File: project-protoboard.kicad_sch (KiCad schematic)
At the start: 8 parts, among them J1 Conn_01x07_Socket, J2 Conn_01x30_Socket, J3 SM04B-SRSS-TB(LF)(SN), J4 Conn_01x05_Socket

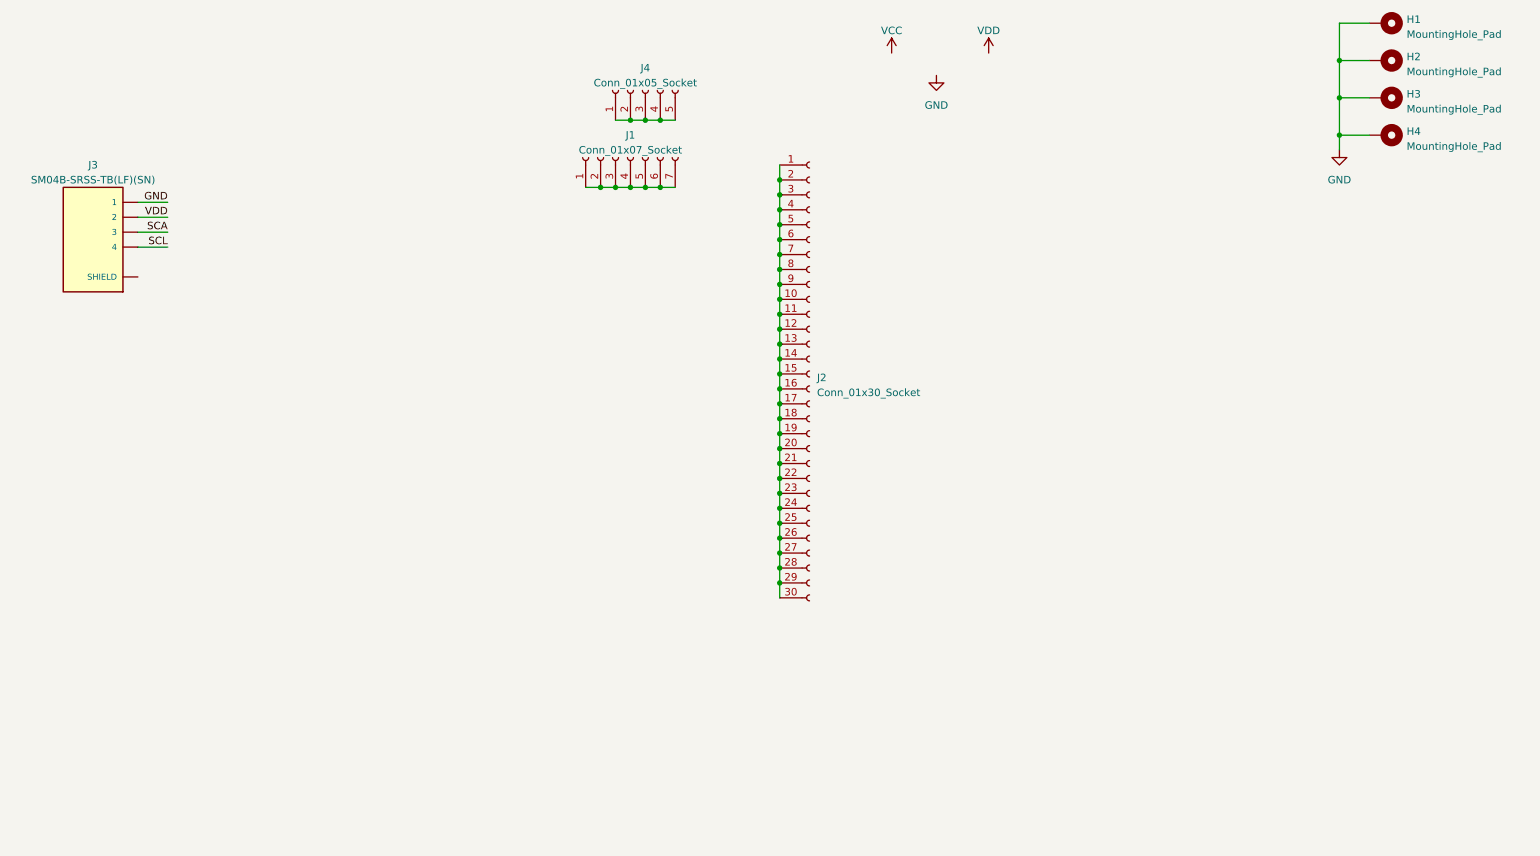
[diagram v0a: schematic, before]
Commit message: Placement and board edge done
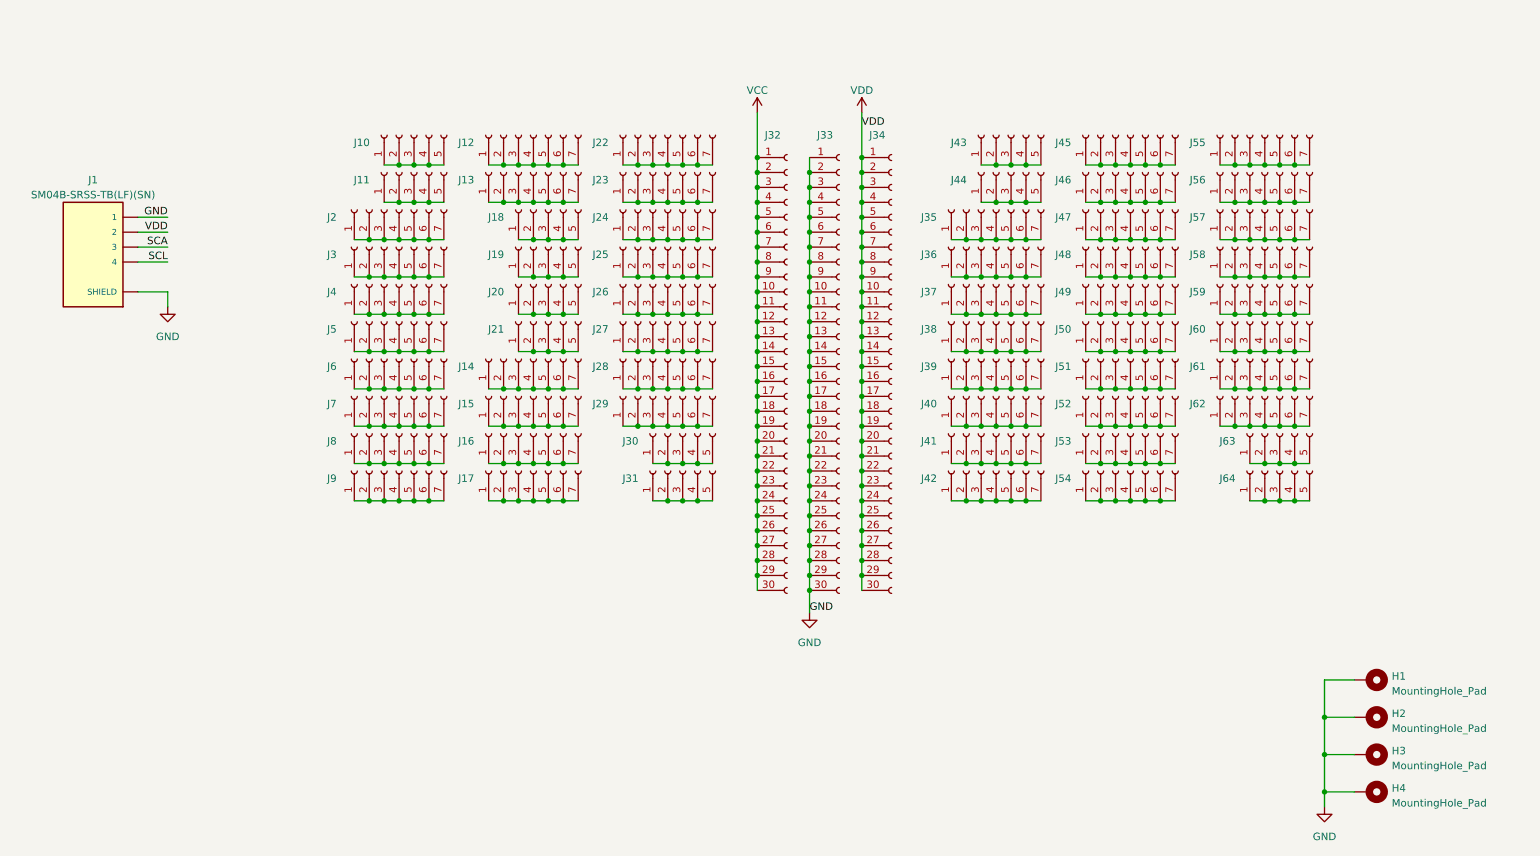
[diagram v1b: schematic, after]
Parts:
- removed J1: Conn_01x07_Socket, Proto:Proto_1x07_P2.54mm, symbol Connector:Conn_01x07_Socket
- added J10, J18, J19, J20, J21, J30, J31, J43, J44, J63, J64: Conn_01x05_Socket, Proto:Proto_1x05_P2.54mm, symbol Connector:Conn_01x05_Socket
- added J12, J13, J14, J15, J16, J17, J2, J22, J23, J24, J25, J26, J27, J28, J29, J3, J35, J36, J37, J38, J39, J4, J40, J41, J42, J45, J46, J47, J48, J49, J5, J50, J51, J52, J53, J54, J55, J56, J57, J58, J59, J6, J60, J61, J62, J7, J8, J9: Conn_01x07_Socket, Proto:Proto_1x07_P2.54mm, symbol Connector:Conn_01x07_Socket
- added J32, J34: Conn_01x30_Socket, Proto:Proto_1x30_P2.54mm, symbol Connector:Conn_01x30_Socket
- renumbered J3 to J1, J4 to J11, J2 to J33
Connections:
- net GND: now also J1.S1 (SHIELD), J1.S2 (SHIELD), J33.1 (Pin_1), J33.10 (Pin_10), J33.11 (Pin_11), J33.12 (Pin_12), J33.13 (Pin_13), J33.14 (Pin_14), J33.15 (Pin_15), J33.16 (Pin_16), J33.17 (Pin_17), J33.18 (Pin_18), J33.19 (Pin_19), J33.2 (Pin_2), J33.20 (Pin_20), J33.21 (Pin_21), J33.22 (Pin_22), J33.23 (Pin_23), J33.24 (Pin_24), J33.25 (Pin_25), J33.26 (Pin_26), J33.27 (Pin_27), J33.28 (Pin_28), J33.29 (Pin_29), J33.3 (Pin_3), J33.30 (Pin_30), J33.4 (Pin_4), J33.5 (Pin_5), J33.6 (Pin_6), J33.7 (Pin_7), J33.8 (Pin_8), J33.9 (Pin_9)
- net VCC: now also J32.1 (Pin_1), J32.10 (Pin_10), J32.11 (Pin_11), J32.12 (Pin_12), J32.13 (Pin_13), J32.14 (Pin_14), J32.15 (Pin_15), J32.16 (Pin_16), J32.17 (Pin_17), J32.18 (Pin_18), J32.19 (Pin_19), J32.2 (Pin_2), J32.20 (Pin_20), J32.21 (Pin_21), J32.22 (Pin_22), J32.23 (Pin_23), J32.24 (Pin_24), J32.25 (Pin_25), J32.26 (Pin_26), J32.27 (Pin_27), J32.28 (Pin_28), J32.29 (Pin_29), J32.3 (Pin_3), J32.30 (Pin_30), J32.4 (Pin_4), J32.5 (Pin_5), J32.6 (Pin_6), J32.7 (Pin_7), J32.8 (Pin_8), J32.9 (Pin_9)
- net VDD: now also J34.1 (Pin_1), J34.10 (Pin_10), J34.11 (Pin_11), J34.12 (Pin_12), J34.13 (Pin_13), J34.14 (Pin_14), J34.15 (Pin_15), J34.16 (Pin_16), J34.17 (Pin_17), J34.18 (Pin_18), J34.19 (Pin_19), J34.2 (Pin_2), J34.20 (Pin_20), J34.21 (Pin_21), J34.22 (Pin_22), J34.23 (Pin_23), J34.24 (Pin_24), J34.25 (Pin_25), J34.26 (Pin_26), J34.27 (Pin_27), J34.28 (Pin_28), J34.29 (Pin_29), J34.3 (Pin_3), J34.30 (Pin_30), J34.4 (Pin_4), J34.5 (Pin_5), J34.6 (Pin_6), J34.7 (Pin_7), J34.8 (Pin_8), J34.9 (Pin_9)
- new net: J39.1 (Pin_1), J39.2 (Pin_2), J39.3 (Pin_3), J39.4 (Pin_4), J39.5 (Pin_5), J39.6 (Pin_6), J39.7 (Pin_7)
- new net: J47.1 (Pin_1), J47.2 (Pin_2), J47.3 (Pin_3), J47.4 (Pin_4), J47.5 (Pin_5), J47.6 (Pin_6), J47.7 (Pin_7)
- new net: J24.1 (Pin_1), J24.2 (Pin_2), J24.3 (Pin_3), J24.4 (Pin_4), J24.5 (Pin_5), J24.6 (Pin_6), J24.7 (Pin_7)
- new net: J30.1 (Pin_1), J30.2 (Pin_2), J30.3 (Pin_3), J30.4 (Pin_4), J30.5 (Pin_5)
- new net: J17.1 (Pin_1), J17.2 (Pin_2), J17.3 (Pin_3), J17.4 (Pin_4), J17.5 (Pin_5), J17.6 (Pin_6), J17.7 (Pin_7)
- new net: J14.1 (Pin_1), J14.2 (Pin_2), J14.3 (Pin_3), J14.4 (Pin_4), J14.5 (Pin_5), J14.6 (Pin_6), J14.7 (Pin_7)
- new net: J62.1 (Pin_1), J62.2 (Pin_2), J62.3 (Pin_3), J62.4 (Pin_4), J62.5 (Pin_5), J62.6 (Pin_6), J62.7 (Pin_7)
- new net: J38.1 (Pin_1), J38.2 (Pin_2), J38.3 (Pin_3), J38.4 (Pin_4), J38.5 (Pin_5), J38.6 (Pin_6), J38.7 (Pin_7)
- new net: J23.1 (Pin_1), J23.2 (Pin_2), J23.3 (Pin_3), J23.4 (Pin_4), J23.5 (Pin_5), J23.6 (Pin_6), J23.7 (Pin_7)
- new net: J6.1 (Pin_1), J6.2 (Pin_2), J6.3 (Pin_3), J6.4 (Pin_4), J6.5 (Pin_5), J6.6 (Pin_6), J6.7 (Pin_7)
- new net: J53.1 (Pin_1), J53.2 (Pin_2), J53.3 (Pin_3), J53.4 (Pin_4), J53.5 (Pin_5), J53.6 (Pin_6), J53.7 (Pin_7)
- new net: J55.1 (Pin_1), J55.2 (Pin_2), J55.3 (Pin_3), J55.4 (Pin_4), J55.5 (Pin_5), J55.6 (Pin_6), J55.7 (Pin_7)
- new net: J3.1 (Pin_1), J3.2 (Pin_2), J3.3 (Pin_3), J3.4 (Pin_4), J3.5 (Pin_5), J3.6 (Pin_6), J3.7 (Pin_7)
- new net: J64.1 (Pin_1), J64.2 (Pin_2), J64.3 (Pin_3), J64.4 (Pin_4), J64.5 (Pin_5)
- new net: J7.1 (Pin_1), J7.2 (Pin_2), J7.3 (Pin_3), J7.4 (Pin_4), J7.5 (Pin_5), J7.6 (Pin_6), J7.7 (Pin_7)
- new net: J25.1 (Pin_1), J25.2 (Pin_2), J25.3 (Pin_3), J25.4 (Pin_4), J25.5 (Pin_5), J25.6 (Pin_6), J25.7 (Pin_7)
- new net: J42.1 (Pin_1), J42.2 (Pin_2), J42.3 (Pin_3), J42.4 (Pin_4), J42.5 (Pin_5), J42.6 (Pin_6), J42.7 (Pin_7)
- new net: J12.1 (Pin_1), J12.2 (Pin_2), J12.3 (Pin_3), J12.4 (Pin_4), J12.5 (Pin_5), J12.6 (Pin_6), J12.7 (Pin_7)
- new net: J57.1 (Pin_1), J57.2 (Pin_2), J57.3 (Pin_3), J57.4 (Pin_4), J57.5 (Pin_5), J57.6 (Pin_6), J57.7 (Pin_7)
- new net: J19.1 (Pin_1), J19.2 (Pin_2), J19.3 (Pin_3), J19.4 (Pin_4), J19.5 (Pin_5)
- new net: J4.1 (Pin_1), J4.2 (Pin_2), J4.3 (Pin_3), J4.4 (Pin_4), J4.5 (Pin_5), J4.6 (Pin_6), J4.7 (Pin_7)
- new net: J43.1 (Pin_1), J43.2 (Pin_2), J43.3 (Pin_3), J43.4 (Pin_4), J43.5 (Pin_5)
- new net: J48.1 (Pin_1), J48.2 (Pin_2), J48.3 (Pin_3), J48.4 (Pin_4), J48.5 (Pin_5), J48.6 (Pin_6), J48.7 (Pin_7)
- new net: J50.1 (Pin_1), J50.2 (Pin_2), J50.3 (Pin_3), J50.4 (Pin_4), J50.5 (Pin_5), J50.6 (Pin_6), J50.7 (Pin_7)
- new net: J46.1 (Pin_1), J46.2 (Pin_2), J46.3 (Pin_3), J46.4 (Pin_4), J46.5 (Pin_5), J46.6 (Pin_6), J46.7 (Pin_7)
- new net: J54.1 (Pin_1), J54.2 (Pin_2), J54.3 (Pin_3), J54.4 (Pin_4), J54.5 (Pin_5), J54.6 (Pin_6), J54.7 (Pin_7)
- new net: J5.1 (Pin_1), J5.2 (Pin_2), J5.3 (Pin_3), J5.4 (Pin_4), J5.5 (Pin_5), J5.6 (Pin_6), J5.7 (Pin_7)
- new net: J52.1 (Pin_1), J52.2 (Pin_2), J52.3 (Pin_3), J52.4 (Pin_4), J52.5 (Pin_5), J52.6 (Pin_6), J52.7 (Pin_7)
- new net: J16.1 (Pin_1), J16.2 (Pin_2), J16.3 (Pin_3), J16.4 (Pin_4), J16.5 (Pin_5), J16.6 (Pin_6), J16.7 (Pin_7)
- new net: J59.1 (Pin_1), J59.2 (Pin_2), J59.3 (Pin_3), J59.4 (Pin_4), J59.5 (Pin_5), J59.6 (Pin_6), J59.7 (Pin_7)
- new net: J63.1 (Pin_1), J63.2 (Pin_2), J63.3 (Pin_3), J63.4 (Pin_4), J63.5 (Pin_5)
- new net: J9.1 (Pin_1), J9.2 (Pin_2), J9.3 (Pin_3), J9.4 (Pin_4), J9.5 (Pin_5), J9.6 (Pin_6), J9.7 (Pin_7)
- new net: J35.1 (Pin_1), J35.2 (Pin_2), J35.3 (Pin_3), J35.4 (Pin_4), J35.5 (Pin_5), J35.6 (Pin_6), J35.7 (Pin_7)
- new net: J29.1 (Pin_1), J29.2 (Pin_2), J29.3 (Pin_3), J29.4 (Pin_4), J29.5 (Pin_5), J29.6 (Pin_6), J29.7 (Pin_7)
- new net: J18.1 (Pin_1), J18.2 (Pin_2), J18.3 (Pin_3), J18.4 (Pin_4), J18.5 (Pin_5)
- new net: J20.1 (Pin_1), J20.2 (Pin_2), J20.3 (Pin_3), J20.4 (Pin_4), J20.5 (Pin_5)
- new net: J58.1 (Pin_1), J58.2 (Pin_2), J58.3 (Pin_3), J58.4 (Pin_4), J58.5 (Pin_5), J58.6 (Pin_6), J58.7 (Pin_7)
- new net: J45.1 (Pin_1), J45.2 (Pin_2), J45.3 (Pin_3), J45.4 (Pin_4), J45.5 (Pin_5), J45.6 (Pin_6), J45.7 (Pin_7)
- new net: J15.1 (Pin_1), J15.2 (Pin_2), J15.3 (Pin_3), J15.4 (Pin_4), J15.5 (Pin_5), J15.6 (Pin_6), J15.7 (Pin_7)
- new net: J26.1 (Pin_1), J26.2 (Pin_2), J26.3 (Pin_3), J26.4 (Pin_4), J26.5 (Pin_5), J26.6 (Pin_6), J26.7 (Pin_7)
- new net: J37.1 (Pin_1), J37.2 (Pin_2), J37.3 (Pin_3), J37.4 (Pin_4), J37.5 (Pin_5), J37.6 (Pin_6), J37.7 (Pin_7)
- new net: J31.1 (Pin_1), J31.2 (Pin_2), J31.3 (Pin_3), J31.4 (Pin_4), J31.5 (Pin_5)
- new net: J8.1 (Pin_1), J8.2 (Pin_2), J8.3 (Pin_3), J8.4 (Pin_4), J8.5 (Pin_5), J8.6 (Pin_6), J8.7 (Pin_7)
- new net: J13.1 (Pin_1), J13.2 (Pin_2), J13.3 (Pin_3), J13.4 (Pin_4), J13.5 (Pin_5), J13.6 (Pin_6), J13.7 (Pin_7)
- new net: J44.1 (Pin_1), J44.2 (Pin_2), J44.3 (Pin_3), J44.4 (Pin_4), J44.5 (Pin_5)
- new net: J60.1 (Pin_1), J60.2 (Pin_2), J60.3 (Pin_3), J60.4 (Pin_4), J60.5 (Pin_5), J60.6 (Pin_6), J60.7 (Pin_7)
- new net: J41.1 (Pin_1), J41.2 (Pin_2), J41.3 (Pin_3), J41.4 (Pin_4), J41.5 (Pin_5), J41.6 (Pin_6), J41.7 (Pin_7)
- new net: J21.1 (Pin_1), J21.2 (Pin_2), J21.3 (Pin_3), J21.4 (Pin_4), J21.5 (Pin_5)
- new net: J28.1 (Pin_1), J28.2 (Pin_2), J28.3 (Pin_3), J28.4 (Pin_4), J28.5 (Pin_5), J28.6 (Pin_6), J28.7 (Pin_7)
- new net: J36.1 (Pin_1), J36.2 (Pin_2), J36.3 (Pin_3), J36.4 (Pin_4), J36.5 (Pin_5), J36.6 (Pin_6), J36.7 (Pin_7)
- new net: J40.1 (Pin_1), J40.2 (Pin_2), J40.3 (Pin_3), J40.4 (Pin_4), J40.5 (Pin_5), J40.6 (Pin_6), J40.7 (Pin_7)
- new net: J51.1 (Pin_1), J51.2 (Pin_2), J51.3 (Pin_3), J51.4 (Pin_4), J51.5 (Pin_5), J51.6 (Pin_6), J51.7 (Pin_7)
- new net: J10.1 (Pin_1), J10.2 (Pin_2), J10.3 (Pin_3), J10.4 (Pin_4), J10.5 (Pin_5)
- new net: J61.1 (Pin_1), J61.2 (Pin_2), J61.3 (Pin_3), J61.4 (Pin_4), J61.5 (Pin_5), J61.6 (Pin_6), J61.7 (Pin_7)
- new net: J2.1 (Pin_1), J2.2 (Pin_2), J2.3 (Pin_3), J2.4 (Pin_4), J2.5 (Pin_5), J2.6 (Pin_6), J2.7 (Pin_7)
- new net: J27.1 (Pin_1), J27.2 (Pin_2), J27.3 (Pin_3), J27.4 (Pin_4), J27.5 (Pin_5), J27.6 (Pin_6), J27.7 (Pin_7)
- new net: J22.1 (Pin_1), J22.2 (Pin_2), J22.3 (Pin_3), J22.4 (Pin_4), J22.5 (Pin_5), J22.6 (Pin_6), J22.7 (Pin_7)
- new net: J49.1 (Pin_1), J49.2 (Pin_2), J49.3 (Pin_3), J49.4 (Pin_4), J49.5 (Pin_5), J49.6 (Pin_6), J49.7 (Pin_7)
- new net: J56.1 (Pin_1), J56.2 (Pin_2), J56.3 (Pin_3), J56.4 (Pin_4), J56.5 (Pin_5), J56.6 (Pin_6), J56.7 (Pin_7)
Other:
- moved on the sheet: H1, H2, H3, H4, J1, J11, J33

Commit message: First complete draft
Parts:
- removed J10, J11, J30, J31, J43, J44, J63, J64: Conn_01x05_Socket, Proto:Proto_1x05_P2.54mm, symbol Connector:Conn_01x05_Socket
- removed J12, J13, J14, J15, J16, J17, J2, J22, J23, J24, J25, J26, J27, J28, J29, J3, J35, J36, J37, J38, J39, J4, J40, J41, J42, J45, J46, J47, J48, J49, J5, J50, J51, J52, J53, J54, J55, J56, J57, J58, J59, J6, J60, J61, J62, J7, J8, J9: Conn_01x07_Socket, Proto:Proto_1x07_P2.54mm, symbol Connector:Conn_01x07_Socket
- removed J34: Conn_01x30_Socket, Proto:Proto_1x30_P2.54mm, symbol Connector:Conn_01x30_Socket
- added J10, J11, J12, J13, J14, J15, J16, J17, J22, J23, J24, J25, J26, J27, J28, J29, J30, J31, J32, J33, J34, J35, J36, J39, J40, J41, J42, J43, J44, J45, J46, J47, J48, J49, J50, J51, J52, J53, J54, J55, J56, J57, J58, J59, J60, J61, J62, J63, J64, J65, J66, J67, J68, J7, J8, J9: Conn_01x06_Socket, Proto:Proto_1x06_P2.54mm, symbol Connector:Conn_01x06_Socket
- added J2: Conn_01x04_Socket, Proto:Proto_1x04_P2.54mm, symbol Connector:Conn_01x04_Socket
- added J3, J5: Conn_01x09_Socket, Proto:Proto_1x09_P2.54mm, symbol Connector:Conn_01x09_Socket
- added J4, J6: Conn_01x13_Socket, Proto:Proto_1x13_P2.54mm, symbol Connector:Conn_01x13_Socket
- added J69, J70: Conn_01x26_Socket, Proto:Proto_1x26_P2.54mm, symbol Connector:Conn_01x26_Socket
- added JP1, JP2, JP3, JP4, JP5, JP6: SolderJumper_2_Open, Jumper:SolderJumper-2_P1.3mm_Open_RoundedPad1.0x1.5mm, symbol Jumper:SolderJumper_2_Open
- renumbered J32 to J37, J33 to J38
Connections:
- net GND: now also J2.1 (Pin_1), JP1.1 (A), JP2.1 (A), JP3.1 (A), JP4.1 (A), JP5.1 (A), JP6.1 (A); no longer J38.1 (Pin_1), J38.10 (Pin_10), J38.11 (Pin_11), J38.12 (Pin_12), J38.13 (Pin_13), J38.14 (Pin_14), J38.15 (Pin_15), J38.16 (Pin_16), J38.17 (Pin_17), J38.18 (Pin_18), J38.19 (Pin_19), J38.2 (Pin_2), J38.20 (Pin_20), J38.21 (Pin_21), J38.22 (Pin_22), J38.23 (Pin_23), J38.24 (Pin_24), J38.25 (Pin_25), J38.26 (Pin_26), J38.27 (Pin_27), J38.28 (Pin_28), J38.29 (Pin_29), J38.3 (Pin_3), J38.30 (Pin_30), J38.4 (Pin_4), J38.5 (Pin_5), J38.6 (Pin_6), J38.7 (Pin_7), J38.8 (Pin_8), J38.9 (Pin_9)
- net SCA: now also J2.3 (Pin_3)
- net SCL: now also J2.4 (Pin_4)
- net VDD: now also J2.2 (Pin_2)
- net VCC: no longer names the net of J37.1 (Pin_1), J37.10 (Pin_10), J37.11 (Pin_11), J37.12 (Pin_12), J37.13 (Pin_13), J37.14 (Pin_14), J37.15 (Pin_15), J37.16 (Pin_16), J37.17 (Pin_17), J37.18 (Pin_18), J37.19 (Pin_19), J37.2 (Pin_2), J37.20 (Pin_20), J37.21 (Pin_21), J37.22 (Pin_22), J37.23 (Pin_23), J37.24 (Pin_24), J37.25 (Pin_25), J37.26 (Pin_26), J37.27 (Pin_27), J37.28 (Pin_28), J37.29 (Pin_29), J37.3 (Pin_3), J37.30 (Pin_30), J37.4 (Pin_4), J37.5 (Pin_5), J37.6 (Pin_6), J37.7 (Pin_7), J37.8 (Pin_8), J37.9 (Pin_9)
- net VCC: now also JP3.2 (B)
- new net: J10.1 (Pin_1), J10.2 (Pin_2), J10.3 (Pin_3), J10.4 (Pin_4), J10.5 (Pin_5), J10.6 (Pin_6)
- new net: J36.1 (Pin_1), J36.2 (Pin_2), J36.3 (Pin_3), J36.4 (Pin_4), J36.5 (Pin_5), J36.6 (Pin_6)
- new net: J26.1 (Pin_1), J26.2 (Pin_2), J26.3 (Pin_3), J26.4 (Pin_4), J26.5 (Pin_5), J26.6 (Pin_6)
- new net: J39.1 (Pin_1), J39.2 (Pin_2), J39.3 (Pin_3), J39.4 (Pin_4), J39.5 (Pin_5), J39.6 (Pin_6)
- new net: J38.1 (Pin_1), J38.10 (Pin_10), J38.11 (Pin_11), J38.12 (Pin_12), J38.13 (Pin_13), J38.14 (Pin_14), J38.15 (Pin_15), J38.16 (Pin_16), J38.17 (Pin_17), J38.18 (Pin_18), J38.19 (Pin_19), J38.2 (Pin_2), J38.20 (Pin_20), J38.21 (Pin_21), J38.22 (Pin_22), J38.23 (Pin_23), J38.24 (Pin_24), J38.25 (Pin_25), J38.26 (Pin_26), J38.27 (Pin_27), J38.28 (Pin_28), J38.29 (Pin_29), J38.3 (Pin_3), J38.30 (Pin_30), J38.4 (Pin_4), J38.5 (Pin_5), J38.6 (Pin_6), J38.7 (Pin_7), J38.8 (Pin_8), J38.9 (Pin_9), JP4.2 (B)
- new net: J70.1 (Pin_1), J70.10 (Pin_10), J70.11 (Pin_11), J70.12 (Pin_12), J70.13 (Pin_13), J70.14 (Pin_14), J70.15 (Pin_15), J70.16 (Pin_16), J70.17 (Pin_17), J70.18 (Pin_18), J70.19 (Pin_19), J70.2 (Pin_2), J70.20 (Pin_20), J70.21 (Pin_21), J70.22 (Pin_22), J70.23 (Pin_23), J70.24 (Pin_24), J70.25 (Pin_25), J70.26 (Pin_26), J70.3 (Pin_3), J70.4 (Pin_4), J70.5 (Pin_5), J70.6 (Pin_6), J70.7 (Pin_7), J70.8 (Pin_8), J70.9 (Pin_9), JP6.2 (B)
- new net: J61.1 (Pin_1), J61.2 (Pin_2), J61.3 (Pin_3), J61.4 (Pin_4), J61.5 (Pin_5), J61.6 (Pin_6)
- new net: J15.1 (Pin_1), J15.2 (Pin_2), J15.3 (Pin_3), J15.4 (Pin_4), J15.5 (Pin_5), J15.6 (Pin_6)
- new net: J54.1 (Pin_1), J54.2 (Pin_2), J54.3 (Pin_3), J54.4 (Pin_4), J54.5 (Pin_5), J54.6 (Pin_6)
- new net: J11.1 (Pin_1), J11.2 (Pin_2), J11.3 (Pin_3), J11.4 (Pin_4), J11.5 (Pin_5), J11.6 (Pin_6)
- new net: J56.1 (Pin_1), J56.2 (Pin_2), J56.3 (Pin_3), J56.4 (Pin_4), J56.5 (Pin_5), J56.6 (Pin_6)
- new net: J55.1 (Pin_1), J55.2 (Pin_2), J55.3 (Pin_3), J55.4 (Pin_4), J55.5 (Pin_5), J55.6 (Pin_6)
- new net: J5.1 (Pin_1), J5.2 (Pin_2), J5.3 (Pin_3), J5.4 (Pin_4), J5.5 (Pin_5), J5.6 (Pin_6), J5.7 (Pin_7), J5.8 (Pin_8), J5.9 (Pin_9), J6.1 (Pin_1), J6.10 (Pin_10), J6.11 (Pin_11), J6.12 (Pin_12), J6.13 (Pin_13), J6.2 (Pin_2), J6.3 (Pin_3), J6.4 (Pin_4), J6.5 (Pin_5), J6.6 (Pin_6), J6.7 (Pin_7), J6.8 (Pin_8), J6.9 (Pin_9), JP2.2 (B)
- new net: J16.1 (Pin_1), J16.2 (Pin_2), J16.3 (Pin_3), J16.4 (Pin_4), J16.5 (Pin_5), J16.6 (Pin_6)
- new net: J3.1 (Pin_1), J3.2 (Pin_2), J3.3 (Pin_3), J3.4 (Pin_4), J3.5 (Pin_5), J3.6 (Pin_6), J3.7 (Pin_7), J3.8 (Pin_8), J3.9 (Pin_9), J4.1 (Pin_1), J4.10 (Pin_10), J4.11 (Pin_11), J4.12 (Pin_12), J4.13 (Pin_13), J4.2 (Pin_2), J4.3 (Pin_3), J4.4 (Pin_4), J4.5 (Pin_5), J4.6 (Pin_6), J4.7 (Pin_7), J4.8 (Pin_8), J4.9 (Pin_9), JP1.2 (B)
- new net: J14.1 (Pin_1), J14.2 (Pin_2), J14.3 (Pin_3), J14.4 (Pin_4), J14.5 (Pin_5), J14.6 (Pin_6)
- new net: J33.1 (Pin_1), J33.2 (Pin_2), J33.3 (Pin_3), J33.4 (Pin_4), J33.5 (Pin_5), J33.6 (Pin_6)
- new net: J53.1 (Pin_1), J53.2 (Pin_2), J53.3 (Pin_3), J53.4 (Pin_4), J53.5 (Pin_5), J53.6 (Pin_6)
- new net: J60.1 (Pin_1), J60.2 (Pin_2), J60.3 (Pin_3), J60.4 (Pin_4), J60.5 (Pin_5), J60.6 (Pin_6)
- new net: J12.1 (Pin_1), J12.2 (Pin_2), J12.3 (Pin_3), J12.4 (Pin_4), J12.5 (Pin_5), J12.6 (Pin_6)
- new net: J24.1 (Pin_1), J24.2 (Pin_2), J24.3 (Pin_3), J24.4 (Pin_4), J24.5 (Pin_5), J24.6 (Pin_6)
- new net: J47.1 (Pin_1), J47.2 (Pin_2), J47.3 (Pin_3), J47.4 (Pin_4), J47.5 (Pin_5), J47.6 (Pin_6)
- new net: J42.1 (Pin_1), J42.2 (Pin_2), J42.3 (Pin_3), J42.4 (Pin_4), J42.5 (Pin_5), J42.6 (Pin_6)
- new net: J50.1 (Pin_1), J50.2 (Pin_2), J50.3 (Pin_3), J50.4 (Pin_4), J50.5 (Pin_5), J50.6 (Pin_6)
- new net: J27.1 (Pin_1), J27.2 (Pin_2), J27.3 (Pin_3), J27.4 (Pin_4), J27.5 (Pin_5), J27.6 (Pin_6)
- new net: J29.1 (Pin_1), J29.2 (Pin_2), J29.3 (Pin_3), J29.4 (Pin_4), J29.5 (Pin_5), J29.6 (Pin_6)
- new net: J65.1 (Pin_1), J65.2 (Pin_2), J65.3 (Pin_3), J65.4 (Pin_4), J65.5 (Pin_5), J65.6 (Pin_6)
- new net: J64.1 (Pin_1), J64.2 (Pin_2), J64.3 (Pin_3), J64.4 (Pin_4), J64.5 (Pin_5), J64.6 (Pin_6)
- new net: J62.1 (Pin_1), J62.2 (Pin_2), J62.3 (Pin_3), J62.4 (Pin_4), J62.5 (Pin_5), J62.6 (Pin_6)
- new net: J40.1 (Pin_1), J40.2 (Pin_2), J40.3 (Pin_3), J40.4 (Pin_4), J40.5 (Pin_5), J40.6 (Pin_6)
- new net: J25.1 (Pin_1), J25.2 (Pin_2), J25.3 (Pin_3), J25.4 (Pin_4), J25.5 (Pin_5), J25.6 (Pin_6)
- new net: J13.1 (Pin_1), J13.2 (Pin_2), J13.3 (Pin_3), J13.4 (Pin_4), J13.5 (Pin_5), J13.6 (Pin_6)
- new net: J58.1 (Pin_1), J58.2 (Pin_2), J58.3 (Pin_3), J58.4 (Pin_4), J58.5 (Pin_5), J58.6 (Pin_6)
- new net: J35.1 (Pin_1), J35.2 (Pin_2), J35.3 (Pin_3), J35.4 (Pin_4), J35.5 (Pin_5), J35.6 (Pin_6)
- new net: J69.1 (Pin_1), J69.10 (Pin_10), J69.11 (Pin_11), J69.12 (Pin_12), J69.13 (Pin_13), J69.14 (Pin_14), J69.15 (Pin_15), J69.16 (Pin_16), J69.17 (Pin_17), J69.18 (Pin_18), J69.19 (Pin_19), J69.2 (Pin_2), J69.20 (Pin_20), J69.21 (Pin_21), J69.22 (Pin_22), J69.23 (Pin_23), J69.24 (Pin_24), J69.25 (Pin_25), J69.26 (Pin_26), J69.3 (Pin_3), J69.4 (Pin_4), J69.5 (Pin_5), J69.6 (Pin_6), J69.7 (Pin_7), J69.8 (Pin_8), J69.9 (Pin_9), JP5.2 (B)
- new net: J46.1 (Pin_1), J46.2 (Pin_2), J46.3 (Pin_3), J46.4 (Pin_4), J46.5 (Pin_5), J46.6 (Pin_6)
- new net: J48.1 (Pin_1), J48.2 (Pin_2), J48.3 (Pin_3), J48.4 (Pin_4), J48.5 (Pin_5), J48.6 (Pin_6)
- new net: J52.1 (Pin_1), J52.2 (Pin_2), J52.3 (Pin_3), J52.4 (Pin_4), J52.5 (Pin_5), J52.6 (Pin_6)
- new net: J57.1 (Pin_1), J57.2 (Pin_2), J57.3 (Pin_3), J57.4 (Pin_4), J57.5 (Pin_5), J57.6 (Pin_6)
- new net: J7.1 (Pin_1), J7.2 (Pin_2), J7.3 (Pin_3), J7.4 (Pin_4), J7.5 (Pin_5), J7.6 (Pin_6)
- new net: J23.1 (Pin_1), J23.2 (Pin_2), J23.3 (Pin_3), J23.4 (Pin_4), J23.5 (Pin_5), J23.6 (Pin_6)
- new net: J8.1 (Pin_1), J8.2 (Pin_2), J8.3 (Pin_3), J8.4 (Pin_4), J8.5 (Pin_5), J8.6 (Pin_6)
- new net: J9.1 (Pin_1), J9.2 (Pin_2), J9.3 (Pin_3), J9.4 (Pin_4), J9.5 (Pin_5), J9.6 (Pin_6)
- new net: J22.1 (Pin_1), J22.2 (Pin_2), J22.3 (Pin_3), J22.4 (Pin_4), J22.5 (Pin_5), J22.6 (Pin_6)
- new net: J34.1 (Pin_1), J34.2 (Pin_2), J34.3 (Pin_3), J34.4 (Pin_4), J34.5 (Pin_5), J34.6 (Pin_6)
- new net: J32.1 (Pin_1), J32.2 (Pin_2), J32.3 (Pin_3), J32.4 (Pin_4), J32.5 (Pin_5), J32.6 (Pin_6)
- new net: J45.1 (Pin_1), J45.2 (Pin_2), J45.3 (Pin_3), J45.4 (Pin_4), J45.5 (Pin_5), J45.6 (Pin_6)
- new net: J67.1 (Pin_1), J67.2 (Pin_2), J67.3 (Pin_3), J67.4 (Pin_4), J67.5 (Pin_5), J67.6 (Pin_6)
- new net: J43.1 (Pin_1), J43.2 (Pin_2), J43.3 (Pin_3), J43.4 (Pin_4), J43.5 (Pin_5), J43.6 (Pin_6)
- new net: J17.1 (Pin_1), J17.2 (Pin_2), J17.3 (Pin_3), J17.4 (Pin_4), J17.5 (Pin_5), J17.6 (Pin_6)
- new net: J41.1 (Pin_1), J41.2 (Pin_2), J41.3 (Pin_3), J41.4 (Pin_4), J41.5 (Pin_5), J41.6 (Pin_6)
- new net: J66.1 (Pin_1), J66.2 (Pin_2), J66.3 (Pin_3), J66.4 (Pin_4), J66.5 (Pin_5), J66.6 (Pin_6)
- new net: J30.1 (Pin_1), J30.2 (Pin_2), J30.3 (Pin_3), J30.4 (Pin_4), J30.5 (Pin_5), J30.6 (Pin_6)
- new net: J44.1 (Pin_1), J44.2 (Pin_2), J44.3 (Pin_3), J44.4 (Pin_4), J44.5 (Pin_5), J44.6 (Pin_6)
- new net: J68.1 (Pin_1), J68.2 (Pin_2), J68.3 (Pin_3), J68.4 (Pin_4), J68.5 (Pin_5), J68.6 (Pin_6)
- new net: J49.1 (Pin_1), J49.2 (Pin_2), J49.3 (Pin_3), J49.4 (Pin_4), J49.5 (Pin_5), J49.6 (Pin_6)
- new net: J63.1 (Pin_1), J63.2 (Pin_2), J63.3 (Pin_3), J63.4 (Pin_4), J63.5 (Pin_5), J63.6 (Pin_6)
- new net: J59.1 (Pin_1), J59.2 (Pin_2), J59.3 (Pin_3), J59.4 (Pin_4), J59.5 (Pin_5), J59.6 (Pin_6)
- new net: J51.1 (Pin_1), J51.2 (Pin_2), J51.3 (Pin_3), J51.4 (Pin_4), J51.5 (Pin_5), J51.6 (Pin_6)
- new net: J28.1 (Pin_1), J28.2 (Pin_2), J28.3 (Pin_3), J28.4 (Pin_4), J28.5 (Pin_5), J28.6 (Pin_6)
- new net: J31.1 (Pin_1), J31.2 (Pin_2), J31.3 (Pin_3), J31.4 (Pin_4), J31.5 (Pin_5), J31.6 (Pin_6)
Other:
- moved on the sheet: J37, J38
